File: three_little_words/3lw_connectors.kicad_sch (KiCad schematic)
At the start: 4 parts, among them J15 Conn_01x17_Female, J16 Conn_01x14_Female, J17 Conn_01x17_Male, J18 Conn_01x14_Male

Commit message: Adding footprints for various components of 3lw.
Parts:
- J15: footprint (none) -> Connector_PinSocket_2.54mm:PinSocket_1x17_P2.54mm_Vertical
- J16: footprint (none) -> Connector_PinSocket_2.54mm:PinSocket_1x14_P2.54mm_Vertical
- J17: footprint (none) -> Connector_PinHeader_2.54mm:PinHeader_1x17_P2.54mm_Vertical
- J18: footprint (none) -> Connector_PinHeader_2.54mm:PinHeader_1x14_P2.54mm_Vertical
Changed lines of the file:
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@@
       (effects (font (size 1.27 1.27)) (justify left))
     )
-    (property "Footprint" "" (id 2) (at 134.112 72.009 0)
+    (property "Footprint" "Connector_PinSocket_2.54mm:PinSocket_1x17_P2.54mm_Vertical" (id 2) (at 134.112 72.009 0)
       (effects (font (size 1.27 1.27)) hide)
     )
@@
     (property "Reference" "J17" (id 0) (at 186.436 45.847 0))
     (property "Value" "Conn_01x17_Male" (id 1) (at 186.436 48.387 0))
-    (property "Footprint" "" (id 2) (at 184.658 72.009 0)
+    (property "Footprint" "Connector_PinHeader_2.54mm:PinHeader_1x17_P2.54mm_Vertical" (id 2) (at 184.658 72.009 0)
       (effects (font (size 1.27 1.27)) hide)
     )
@@
       (effects (font (size 1.27 1.27)) (justify left))
     )
-    (property "Footprint" "" (id 2) (at 134.112 121.285 0)
+    (property "Footprint" "Connector_PinSocket_2.54mm:PinSocket_1x14_P2.54mm_Vertical" (id 2) (at 134.112 121.285 0)
       (effects (font (size 1.27 1.27)) hide)
     )
@@
     (property "Reference" "J18" (id 0) (at 187.96 100.203 0))
     (property "Value" "Conn_01x14_Male" (id 1) (at 187.96 102.743 0))
-    (property "Footprint" "" (id 2) (at 185.166 121.285 0)
+    (property "Footprint" "Connector_PinHeader_2.54mm:PinHeader_1x14_P2.54mm_Vertical" (id 2) (at 185.166 121.285 0)
       (effects (font (size 1.27 1.27)) hide)
     )

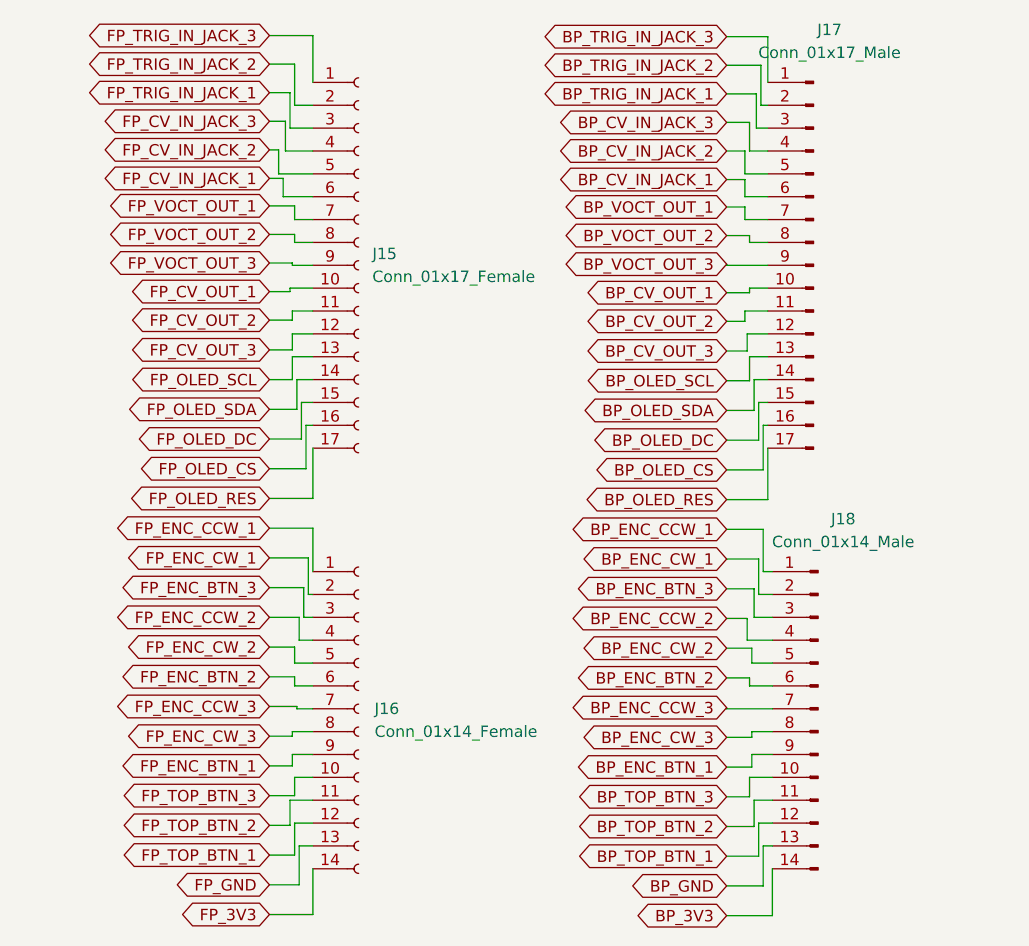
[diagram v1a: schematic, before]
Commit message: Tried to sort circuit. Mixed success.
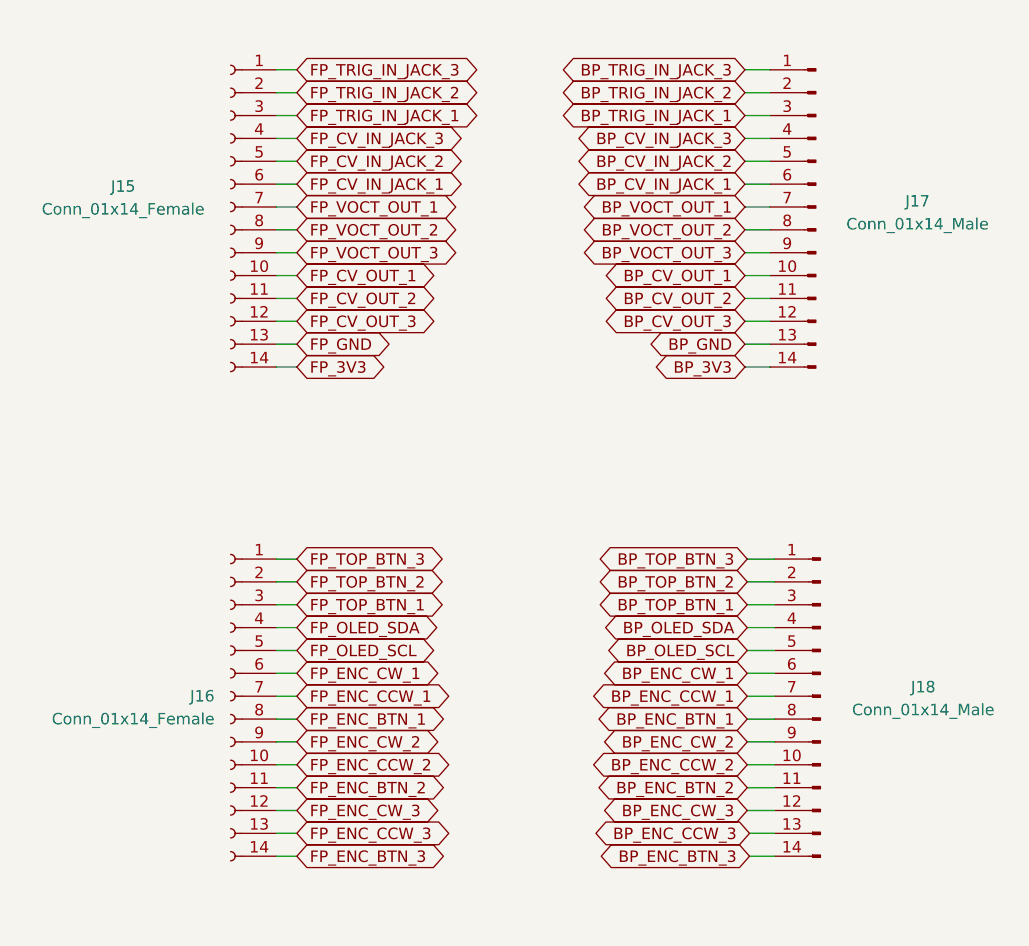
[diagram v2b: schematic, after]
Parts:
- J15: value Conn_01x17_Female -> Conn_01x14_Female; footprint Connector_PinSocket_2.54mm:PinSocket_1x17_P2.54mm_Vertical -> Connector_PinSocket_2.54mm:PinSocket_1x14_P2.54mm_Vertical; symbol Connector:Conn_01x17_Female -> Connector:Conn_01x14_Female
- J17: value Conn_01x17_Male -> Conn_01x14_Male; footprint Connector_PinHeader_2.54mm:PinHeader_1x17_P2.54mm_Vertical -> Connector_PinHeader_2.54mm:PinHeader_1x14_P2.54mm_Vertical; symbol Connector:Conn_01x17_Male -> Connector:Conn_01x14_Male
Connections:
- net BP_3V3: now also J17.14 (Pin_14); no longer J18.14 (Pin_14)
- net BP_ENC_BTN_1: now also J18.8 (Pin_8); no longer J18.9 (Pin_9)
- net BP_ENC_BTN_2: now also J18.11 (Pin_11); no longer J18.6 (Pin_6)
- net BP_ENC_BTN_3: now also J18.14 (Pin_14); no longer J18.3 (Pin_3)
- net BP_ENC_CCW_1: now also J18.7 (Pin_7); no longer J18.1 (Pin_1)
- net BP_ENC_CCW_2: now also J18.10 (Pin_10); no longer J18.4 (Pin_4)
- net BP_ENC_CCW_3: now also J18.13 (Pin_13); no longer J18.7 (Pin_7)
- net BP_ENC_CW_1: now also J18.6 (Pin_6); no longer J18.2 (Pin_2)
- net BP_ENC_CW_2: now also J18.9 (Pin_9); no longer J18.5 (Pin_5)
- net BP_ENC_CW_3: now also J18.12 (Pin_12); no longer J18.8 (Pin_8)
- net BP_GND: now also J17.13 (Pin_13); no longer J18.13 (Pin_13)
- net BP_OLED_SCL: now also J18.5 (Pin_5); no longer J17.13 (Pin_13)
- net BP_OLED_SDA: now also J18.4 (Pin_4); no longer J17.14 (Pin_14)
- net BP_TOP_BTN_1: now also J18.3 (Pin_3); no longer J18.12 (Pin_12)
- net BP_TOP_BTN_2: now also J18.2 (Pin_2); no longer J18.11 (Pin_11)
- net BP_TOP_BTN_3: now also J18.1 (Pin_1); no longer J18.10 (Pin_10)
- net FP_3V3: now also J15.14 (Pin_14); no longer J16.14 (Pin_14)
- net FP_ENC_BTN_1: now also J16.8 (Pin_8); no longer J16.9 (Pin_9)
- net FP_ENC_BTN_2: now also J16.11 (Pin_11); no longer J16.6 (Pin_6)
- net FP_ENC_BTN_3: now also J16.14 (Pin_14); no longer J16.3 (Pin_3)
- net FP_ENC_CCW_1: now also J16.7 (Pin_7); no longer J16.1 (Pin_1)
- net FP_ENC_CCW_2: now also J16.10 (Pin_10); no longer J16.4 (Pin_4)
- net FP_ENC_CCW_3: now also J16.13 (Pin_13); no longer J16.7 (Pin_7)
- net FP_ENC_CW_1: now also J16.6 (Pin_6); no longer J16.2 (Pin_2)
- net FP_ENC_CW_2: now also J16.9 (Pin_9); no longer J16.5 (Pin_5)
- net FP_ENC_CW_3: now also J16.12 (Pin_12); no longer J16.8 (Pin_8)
- net FP_GND: now also J15.13 (Pin_13); no longer J16.13 (Pin_13)
- net FP_OLED_SCL: now also J16.5 (Pin_5); no longer J15.13 (Pin_13)
- net FP_OLED_SDA: now also J16.4 (Pin_4); no longer J15.14 (Pin_14)
- net FP_TOP_BTN_1: now also J16.3 (Pin_3); no longer J16.12 (Pin_12)
- net FP_TOP_BTN_2: now also J16.2 (Pin_2); no longer J16.11 (Pin_11)
- net FP_TOP_BTN_3: now also J16.1 (Pin_1); no longer J16.10 (Pin_10)
- removed net BP_OLED_CS: J17.16 (Pin_16)
- removed net BP_OLED_DC: J17.15 (Pin_15)
- removed net BP_OLED_RES: J17.17 (Pin_17)
- removed net FP_OLED_CS: J15.16 (Pin_16)
- removed net FP_OLED_DC: J15.15 (Pin_15)
- removed net FP_OLED_RES: J15.17 (Pin_17)
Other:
- moved on the sheet: J16, J18
